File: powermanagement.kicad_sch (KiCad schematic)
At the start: 29 parts, among them J9 Battery, Q2 AP2302B, SW6 SW_SPDT, U4 SY8079AAC, U5 XT4054K421MR-G, U6 SY6280AAC

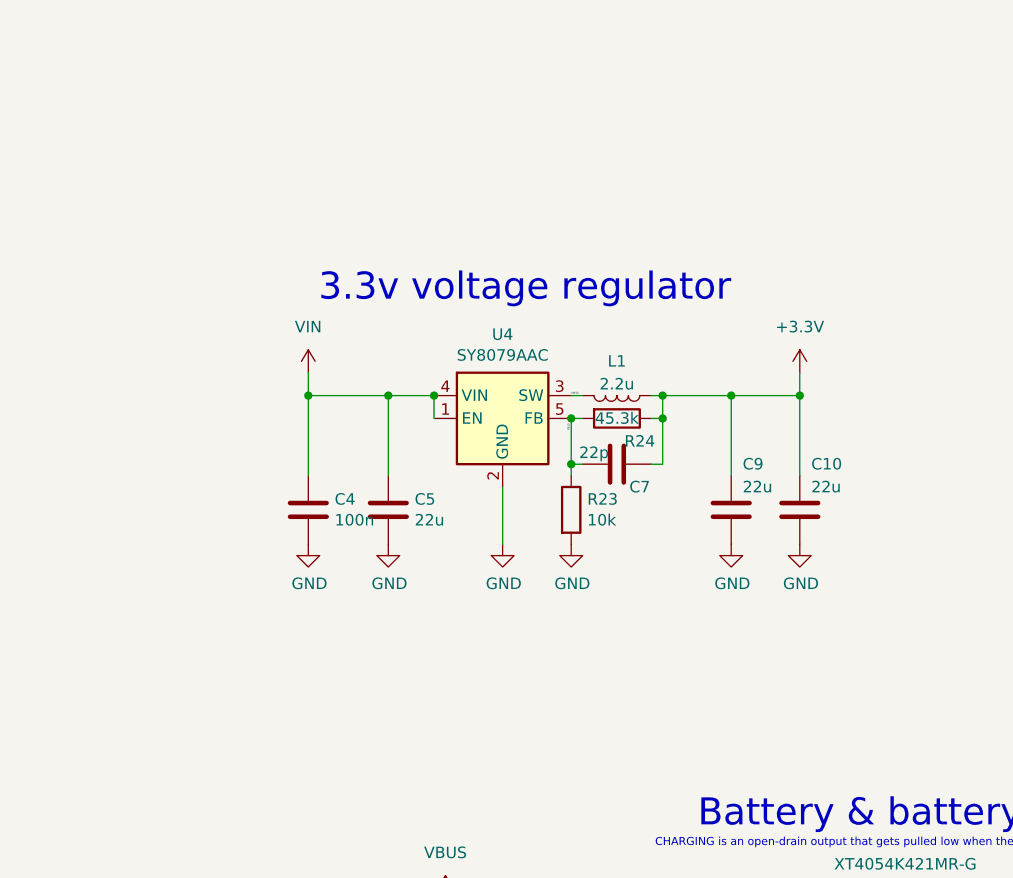
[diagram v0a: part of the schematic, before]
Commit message: Use DC/DC from WHY badge
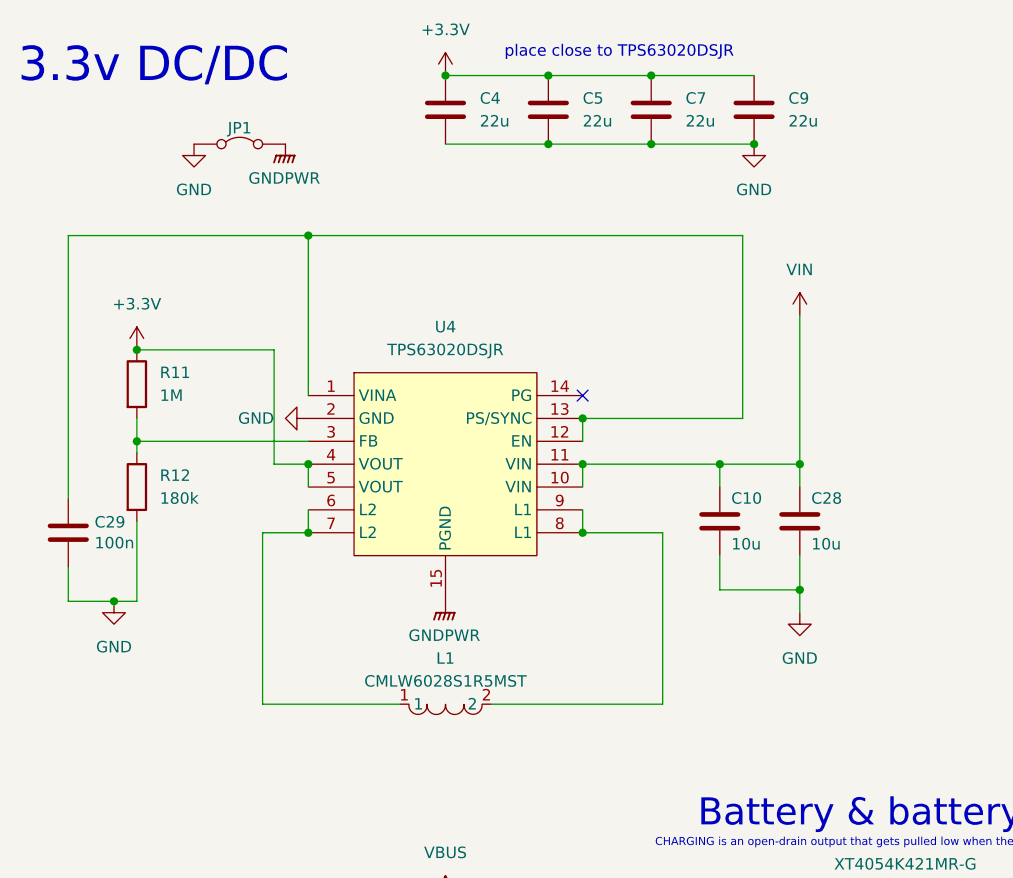
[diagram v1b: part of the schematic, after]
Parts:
- removed C10, C5, C9: 22u, Capacitor_SMD:C_0805_2012Metric, symbol symbols:C
- removed C4: 100n, Capacitor_SMD:C_0402_1005Metric, symbol symbols:C
- removed C7: 22p, Capacitor_SMD:C_0402_1005Metric, symbol symbols:C
- removed L1: 2.2u, library:Inductor_MSC20FC, symbol symbols:L
- removed R23: 10k, Resistor_SMD:R_0402_1005Metric, symbol symbols:R
- removed R24: 45.3k, Resistor_SMD:R_0402_1005Metric, symbol symbols:R
- removed U4: SY8079AAC, library:SOT-23-5, symbol symbols:TLV62568DBV-Regulator_Switching
- added C10, C28: 10u, Capacitor_SMD:C_0805_2012Metric, symbol Device:C
- added C29: 100n, Capacitor_SMD:C_0402_1005Metric, symbol symbols:C
- added C4, C5, C7, C9: 22u, Capacitor_SMD:C_0805_2012Metric, symbol Device:C
- added JP1: ~, NetTie:NetTie-2_SMD_Pad0.5mm, symbol Jumper:Jumper_2_Bridged
- added L1: CMLW6028S1R5MST, library:IND-SMD_L6.0-W6.0, symbol lcsc:CMLW6028S1R5MST
- added R11: 1M, Resistor_SMD:R_0402_1005Metric_Pad0.72x0.64mm_HandSolder, symbol Device:R
- added R12: 180k, Resistor_SMD:R_0402_1005Metric_Pad0.72x0.64mm_HandSolder, symbol Device:R
- added U4: TPS63020DSJR, library:VSON-14_L4.0-W3.0-P0.50-BL-EP_TI_DSJ, symbol lcsc:TPS63020DSJR
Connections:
- net +3.3V: now also C4.1, C5.1, C7.1, C9.1, R11.1, U4.4 (VOUT), U4.5 (VOUT)
- net GND: now also C10.2, C28.2, C29.2, C4.2, C5.2, C7.2, C9.2, JP1.1 (A), R12.2, U4.2 (GND)
- net VIN: now also C10.1, C28.1, U4.10 (VIN), U4.11 (VIN)
- new net: L1.1, U4.6 (L2), U4.7 (L2)
- new net: L1.2, U4.8 (L1), U4.9 (L1)
- new net: C29.1, U4.1 (VINA), U4.12 (EN), U4.13 (PS/SYNC)
- new net: R11.2, R12.1, U4.3 (FB)
- new net GNDPWR: JP1.2 (B), U4.15 (PGND)
- no-connect marks 0 -> 1
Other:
- note added: "3.3v DC/DC"
- note added: "place close to TPS63020DSJR"
- note removed: "3.3v voltage regulator"

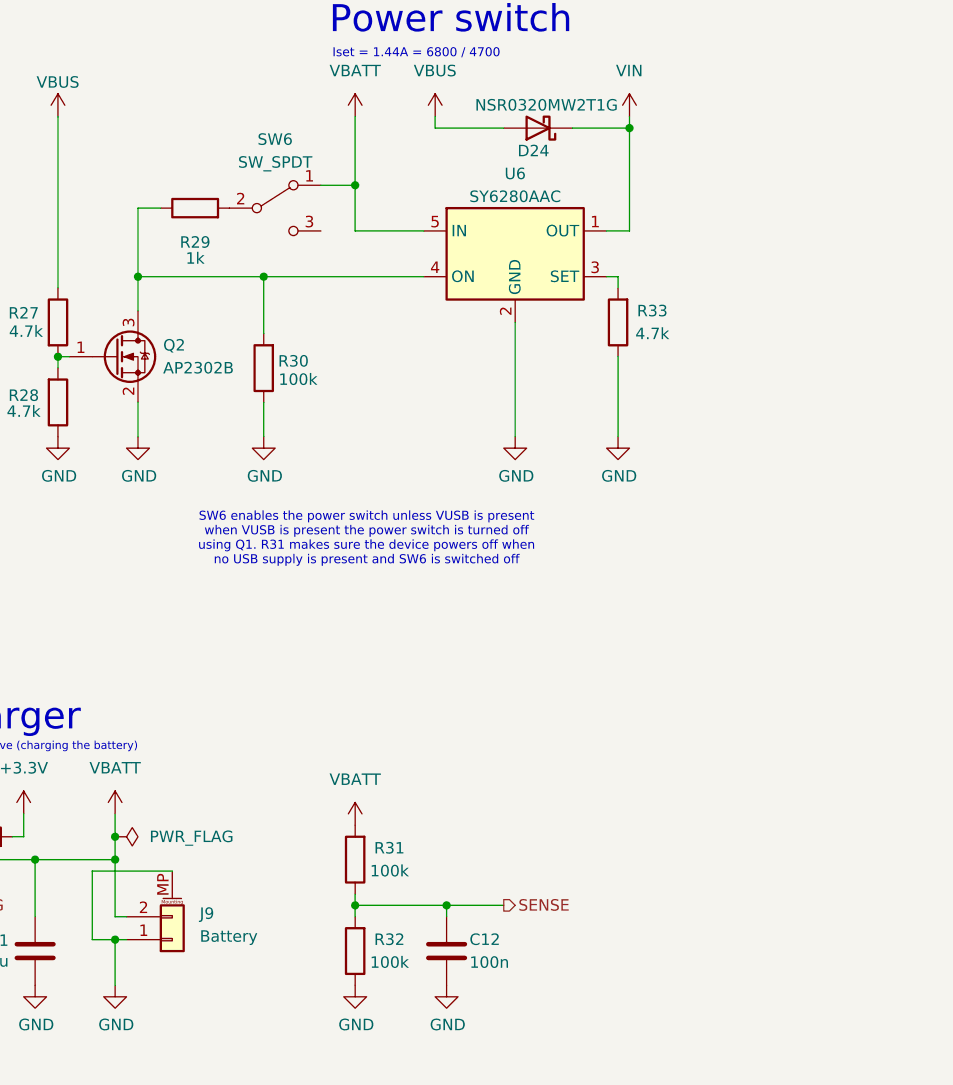
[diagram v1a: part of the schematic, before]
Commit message: No DRC errors
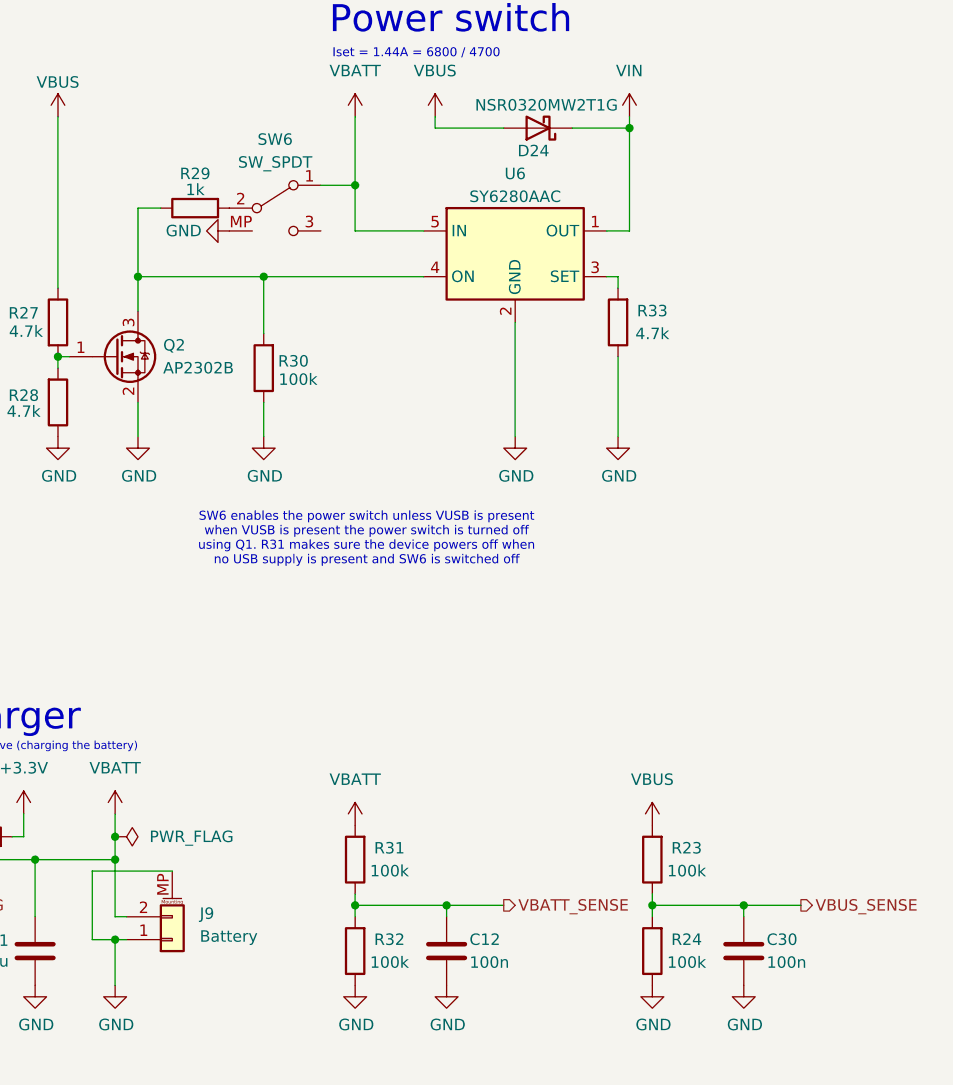
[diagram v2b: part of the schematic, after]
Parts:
- added C30: 100n, Capacitor_SMD:C_0402_1005Metric, symbol symbols:C
- added R23, R24: 100k, Resistor_SMD:R_0402_1005Metric, symbol symbols:R
- SW6: footprint Button_Switch_SMD:SW_SPDT_PCM12 -> library:SW_SPDT_PCM12_MP; symbol Switch:SW_SPDT -> library:SW_SPDT_MP
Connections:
- net GND: now also SW6.MP, C30.2, R24.1
- net VBUS: now also R23.2
- net SENSE renamed VBATT_SENSE
- new net VBUS_SENSE: C30.1, R23.1, R24.2

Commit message: Cleanup & tweaks
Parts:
- C10, C28: LCSC C3039694 -> (none)
- C11, C6: LCSC C5189822 -> (none)
- C29: LCSC C307331 -> (none)
- C4, C5, C7, C9: LCSC C45783 -> (none)

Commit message: Fill out BOM, add labels to PCB
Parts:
- C10, C11, C28, C6: LCSC (none) -> C3039694
- C12, C29, C30, C8: LCSC (none) -> C307331
- C4, C5, C7, C9: LCSC (none) -> C45783
- R23, R24, R30, R31, R32: LCSC (none) -> C25741
- R25: LCSC (none) -> C4109
- R26: LCSC (none) -> C25744
- R27, R28, R33: LCSC (none) -> C25940
- R29: LCSC (none) -> C11702
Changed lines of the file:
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@@
 			)
 		)
-		(property "Datasheet" "https://datasheet.lcsc.com/lcsc/1912300933_TORCH-C0805B104K500NT_C476766.pdf"
+		(property "Datasheet" "https://datasheet.lcsc.com/lcsc/2304140030_Samsung-Electro-Mechanics-CL05B104KB54PNC_C307331.pdf"
 			(at 200.66 135.89 0)
 			(effects
@@
 			)
 		)
-		(property "LCSC" ""
+		(property "LCSC" "C307331"
 			(at 200.66 135.89 0)
 			(effects
@@
 			)
 		)
-		(property "Datasheet" "https://datasheet.lcsc.com/lcsc/1912300933_TORCH-C0805B104K500NT_C476766.pdf"
+		(property "Datasheet" "https://datasheet.lcsc.com/lcsc/2304140030_Samsung-Electro-Mechanics-CL05B104KB54PNC_C307331.pdf"
 			(at 104.14 135.89 0)
 			(effects
@@
 			)
 		)
-		(property "LCSC" ""
+		(property "LCSC" "C307331"
 			(at 104.14 135.89 0)
 			(effects
@@
 			)
 		)
-		(property "Datasheet" "https://datasheet.lcsc.com/lcsc/1912300933_TORCH-C0805B104K500NT_C476766.pdf"
+		(property "Datasheet" "https://datasheet.lcsc.com/lcsc/2304140030_Samsung-Electro-Mechanics-CL05B104KB54PNC_C307331.pdf"
 			(at 233.68 135.89 0)
 			(effects
@@
 			)
 		)
-		(property "LCSC" ""
+		(property "LCSC" "C307331"
 			(at 233.68 135.89 0)
 			(effects
@@
 			)
 		)
-		(property "Datasheet" "https://datasheet.lcsc.com/lcsc/2110151630_XKB-Connectivity-SK-3296S-01-L1_C319020.pdf"
+		(property "Datasheet" "https://www.lcsc.com/product-detail/Slide-Switches_XKB-Connection-SK-3296S-01-L1_C319020.html"
 			(at 184.404 66.548 0)
 			(effects
@@
 			)
 		)
-		(property "Datasheet" "https://datasheet.lcsc.com/lcsc/2308241947_FOJAN-FRC0805J104-TS_C2907293.pdf"
+		(property "Datasheet" "https://www.lcsc.com/product-detail/Chip-Resistor-Surface-Mount_UNI-ROYAL-Uniroyal-Elec-0402WGF1003TCE_C25741.html"
 			(at 223.52 125.73 0)
 			(effects
@@
 			)
 		)
-		(property "LCSC" ""
+		(property "LCSC" "C25741"
 			(at 223.52 125.73 0)
 			(effects
@@
 			)
 		)
-		(property "Datasheet" ""
+		(property "Datasheet" "https://www.lcsc.com/product-detail/Chip-Resistor-Surface-Mount_UNI-ROYAL-Uniroyal-Elec-0402WGJ0472TCE_C25940.html"
 			(at 157.48 66.04 0)
 			(effects
@@
 			)
 		)
-		(property "LCSC" ""
+		(property "LCSC" "C25940"
 			(at 157.48 66.04 0)
 			(effects
@@
 			)
 		)
-		(property "Datasheet" "https://datasheet.lcsc.com/lcsc/2308241947_FOJAN-FRC0805J472-TS_C2907326.pdf"
+		(property "Datasheet" "https://www.lcsc.com/product-detail/Chip-Resistor-Surface-Mount_UNI-ROYAL-Uniroyal-Elec-0402WGJ0472TCE_C25940.html"
 			(at 219.71 66.04 0)
 			(effects
@@
 			)
 		)
-		(property "LCSC" ""
+		(property "LCSC" "C25940"
 			(at 219.71 66.04 0)
 			(effects
@@
 			)
 		)
-		(property "Datasheet" "https://datasheet.lcsc.com/lcsc/2308241947_FOJAN-FRC0805J104-TS_C2907293.pdf"
+		(property "Datasheet" "https://www.lcsc.com/product-detail/Chip-Resistor-Surface-Mount_UNI-ROYAL-Uniroyal-Elec-0402WGF1003TCE_C25741.html"
 			(at 190.5 125.73 0)
 			(effects
@@
 			)
 		)
-		(property "LCSC" ""
+		(property "LCSC" "C25741"
 			(at 190.5 125.73 0)
 			(effects
@@
 			)
 		)
-		(property "Datasheet" ""
+		(property "Datasheet" "https://www.lcsc.com/product-detail/Chip-Resistor-Surface-Mount_UNI-ROYAL-Uniroyal-Elec-0402WGF1001TCE_C11702.html"
 			(at 172.72 53.34 0)
 			(effects
@@
 			)
 		)
-		(property "LCSC" ""
+		(property "LCSC" "C11702"
 			(at 172.72 53.34 0)
 			(effects
@@
 			)
 		)
-		(property "Datasheet" "https://datasheet.lcsc.com/lcsc/2308241947_FOJAN-FRC0805J104-TS_C2907293.pdf"
+		(property "Datasheet" "https://www.lcsc.com/product-detail/Chip-Resistor-Surface-Mount_UNI-ROYAL-Uniroyal-Elec-0402WGF1003TCE_C25741.html"
 			(at 180.34 71.12 0)
 			(effects
@@
 			)
 		)
-		(property "LCSC" ""
+		(property "LCSC" "C25741"
 			(at 180.34 71.12 0)
 			(effects
@@
 			)
 		)
-		(property "LCSC" ""
+		(property "LCSC" "C45783"
 			(at 101.6 31.75 0)
 			(effects
@@
 			)
 		)
-		(property "LCSC" ""
+		(property "LCSC" "C3039694"
 			(at 118.11 77.47 0)
 			(effects
@@
 			)
 		)
-		(property "LCSC" ""
+		(property "LCSC" "C307331"
 			(at 36.83 78.74 0)
 			(effects
@@
 			)
 		)
-		(property "Datasheet" "https://datasheet.lcsc.com/lcsc/2205131800_VO-SCR0805J2K_C3017846.pdf"
+		(property "Datasheet" "https://www.lcsc.com/product-detail/Chip-Resistor-Surface-Mount_UNI-ROYAL-Uniroyal-Elec-0402WGF2001TCE_C4109.html"
 			(at 116.84 130.81 0)
 			(effects
@@
 			)
 		)
-		(property "LCSC" ""
+		(property "LCSC" "C4109"
 			(at 116.84 130.81 0)
 			(effects
@@
 			)
 		)
-		(property "Datasheet" "https://wmsc.lcsc.com/wmsc/upload/file/pdf/v2/lcsc/2206010030_UNI-ROYAL-Uniroyal-Elec-0402WGF1004TCE_C26083.pdf"
+		(property "Datasheet" "https://www.lcsc.com/product-detail/Chip-Resistor-Surface-Mount_UNI-ROYAL-Uniroyal-Elec-0402WGF1004TCE_C26083.html"
 			(at 44.45 62.23 0)
 			(effects
@@
 			)
 		)
-		(property "Datasheet" "https://datasheet.lcsc.com/lcsc/2308241947_FOJAN-FRC0805J104-TS_C2907293.pdf"
+		(property "Datasheet" "https://www.lcsc.com/product-detail/Chip-Resistor-Surface-Mount_UNI-ROYAL-Uniroyal-Elec-0402WGF1003TCE_C25741.html"
 			(at 223.52 135.89 0)
 			(effects
@@
 			)
 		)
-		(property "LCSC" ""
+		(property "LCSC" "C25741"
 			(at 223.52 135.89 0)
 			(effects
@@
 			)
 		)
-		(property "LCSC" ""
+		(property "LCSC" "C3039694"
 			(at 109.22 77.47 0)
 			(effects
@@
 			)
 		)
-		(property "LCSC" ""
+		(property "LCSC" "C45783"
 			(at 78.74 31.75 0)
 			(effects
@@
 			)
 		)
-		(property "Datasheet" "https://datasheet.lcsc.com/lcsc/2210121101_Samwha-Capacitor-CS2012X7R106M100NRE_C5189822.pdf"
+		(property "Datasheet" "https://www.lcsc.com/product-detail/Multilayer-Ceramic-Capacitors-MLCC-SMD-SMT_Samsung-Electro-Mechanics-CL21B106KAYQNNE_C3039694.html"
 			(at 154.94 135.89 0)
 			(effects
@@
 			)
 		)
-		(property "LCSC" ""
+		(property "LCSC" "C3039694"
 			(at 154.94 135.89 0)
 			(effects
@@
 			)
 		)
-		(property "LCSC" ""
+		(property "LCSC" "C45783"
 			(at 113.03 31.75 0)
 			(effects
@@
 			)
 		)
-		(property "LCSC" ""
+		(property "LCSC" "C45783"
 			(at 90.17 31.75 0)
 			(effects
@@
 			)
 		)
-		(property "Datasheet" "https://datasheet.lcsc.com/lcsc/2210121101_Samwha-Capacitor-CS2012X7R106M100NRE_C5189822.pdf"
+		(property "Datasheet" "https://www.lcsc.com/product-detail/Multilayer-Ceramic-Capacitors-MLCC-SMD-SMT_Samsung-Electro-Mechanics-CL21B106KAYQNNE_C3039694.html"
 			(at 93.98 135.89 0)
 			(effects
@@
 			)
 		)
-		(property "LCSC" ""
+		(property "LCSC" "C3039694"
 			(at 93.98 135.89 0)
 			(effects
@@
 			)
 		)
-		(property "Datasheet" ""
+		(property "Datasheet" "https://www.lcsc.com/product-detail/Chip-Resistor-Surface-Mount_UNI-ROYAL-Uniroyal-Elec-0402WGJ0472TCE_C25940.html"
 			(at 157.48 74.93 0)
 			(effects
@@
 			)
 		)
-		(property "LCSC" ""
+		(property "LCSC" "C25940"
 			(at 157.48 74.93 0)
 			(effects
@@
 			)
 		)
-		(property "Datasheet" "https://jlcpcb.com/partdetail/Fojan-FRC0402F1803TS/C2909325"
+		(property "Datasheet" "https://www.lcsc.com/product-detail/Chip-Resistor-Surface-Mount_FOJAN-FRC0402F1803TS_C2909325.html"
 			(at 44.45 73.66 0)
 			(effects
@@
 			)
 		)
-		(property "Datasheet" "https://datasheet.lcsc.com/lcsc/2208231730_VO-SCR0805J10K_C5140188.pdf"
+		(property "Datasheet" "https://www.lcsc.com/product-detail/Chip-Resistor-Surface-Mount_UNI-ROYAL-Uniroyal-Elec-0402WGF1002TCE_C25744.html"
 			(at 148.59 123.19 0)
 			(effects
@@
 			)
 		)
-		(property "LCSC" ""
+		(property "LCSC" "C25744"
 			(at 148.59 123.19 0)
 			(effects
@@
 			)
 		)
-		(property "Datasheet" "https://datasheet.lcsc.com/lcsc/2308241947_FOJAN-FRC0805J104-TS_C2907293.pdf"
+		(property "Datasheet" "https://www.lcsc.com/product-detail/Chip-Resistor-Surface-Mount_UNI-ROYAL-Uniroyal-Elec-0402WGF1003TCE_C25741.html"
 			(at 190.5 135.89 0)
 			(effects
@@
 			)
 		)
-		(property "LCSC" ""
+		(property "LCSC" "C25741"
 			(at 190.5 135.89 0)
 			(effects

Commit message: Changes for production version
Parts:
- U6: footprint library:SOT-23-5 -> Package_TO_SOT_SMD:SOT-23-5
